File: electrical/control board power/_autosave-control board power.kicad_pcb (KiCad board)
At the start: 2 copper layers, 147.3 x 147.3 mm, 67 parts, among them J1 Conn_01x02, J10 48V_from_conversion, J11 Aux_2, J17 Switch_B, J2 5V, J3 Barrel_Jack, J4 Switch_A, J5 Switch_Input, J6 Power_Connector, J7 Switch_A_High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

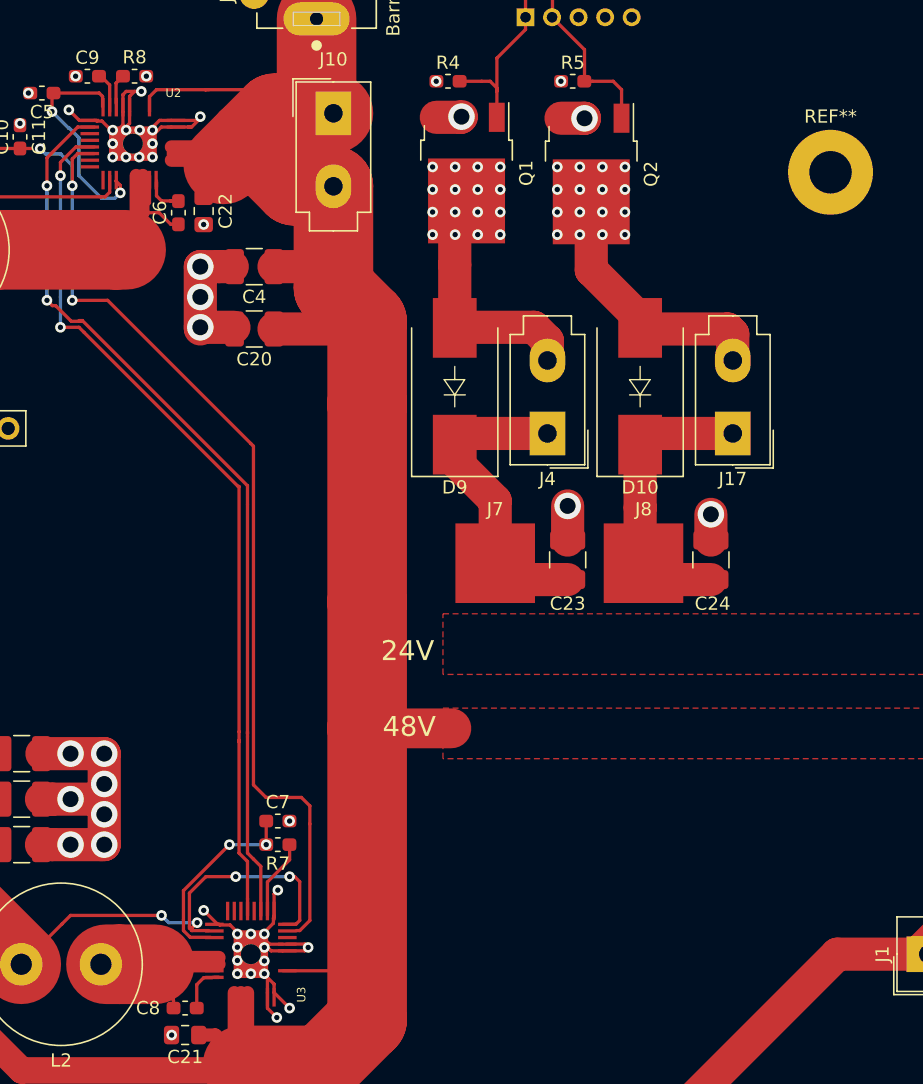
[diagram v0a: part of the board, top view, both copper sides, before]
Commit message: Added parts to board
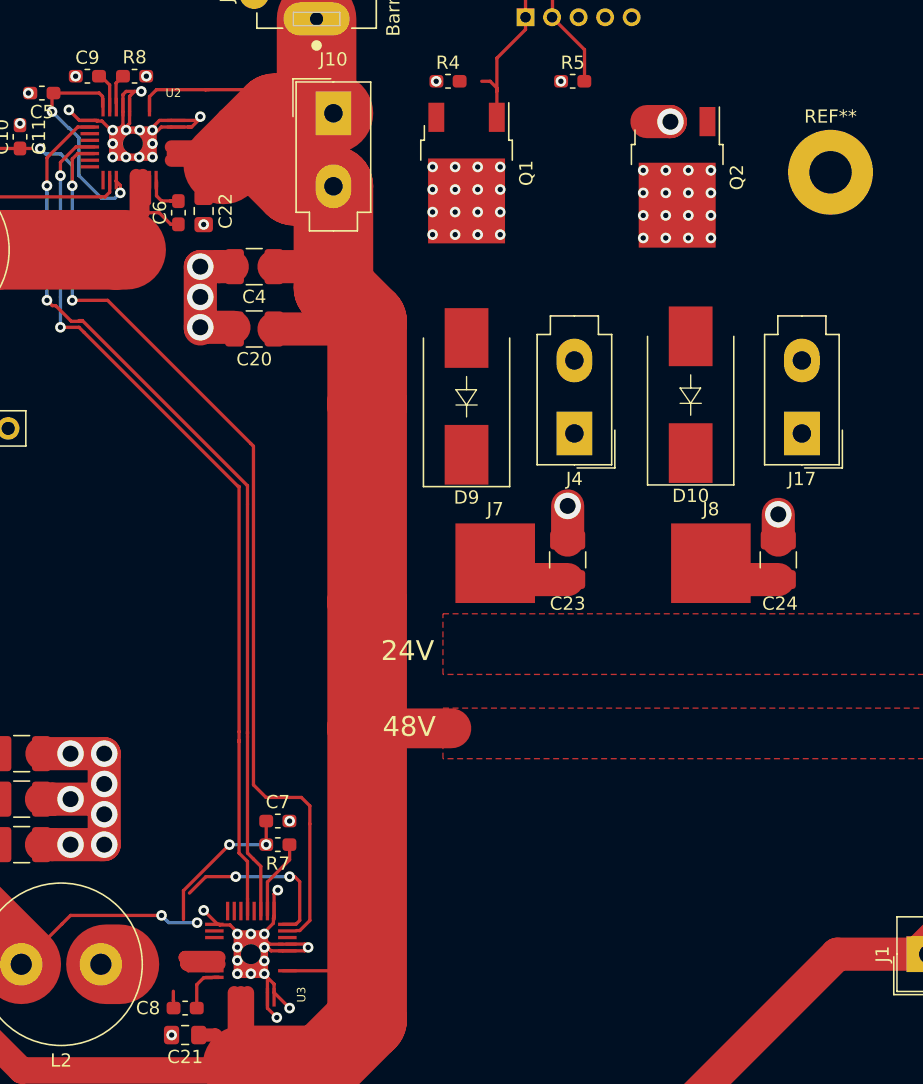
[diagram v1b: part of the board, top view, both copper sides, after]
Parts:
- moved Q2 6.48 mm to (132.0, 63.1)
- moved J17 5.21 mm to (141.4, 82.4)
- moved C24 5.08 mm to (139.6, 91.9)
- moved J8 5.08 mm to (134.5, 87.6)
- moved D10 3.86 mm to (133.0, 79.5)
- moved J4 2.03 mm to (124.2, 82.4)
- moved D9 1.17 mm to (116.1, 79.6)
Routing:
- net Net-(D10-Pad2): track 19.9 -> 0.00 mm
- net Net-(D9-Pad2): track 18.8 -> 1.62 mm
- net /SWITCH_A_HIGH: track 19.6 -> 3.32 mm
- net /SWITCH_B_HIGH: track 18.3 -> 3.19 mm
- net /SWITCH_B: track 16.4 -> 11.5 mm
- net +5V: track 289.4 -> 284.4 mm
- net Net-(C7-Pad1): track 14.7 -> 11.6 mm
- net Net-(C8-Pad2): track 12.4 -> 9.75 mm
- net Net-(C23-Pad1): track 8.21 -> 6.29 mm, vias 6 -> 5
- net /SWITCH_A: track 19.3 -> 17.6 mm
